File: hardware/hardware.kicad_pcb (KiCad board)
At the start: 2 copper layers, 85.5 x 50.5 mm, 22 parts, among them J1 Conn_01x05_Male, J2 DIN-5_180degree, SW1 SW_Push, SW2 SW_Push, U1 Teensy3.2, U2 TeensyAudioShield3.2, U3 6N138

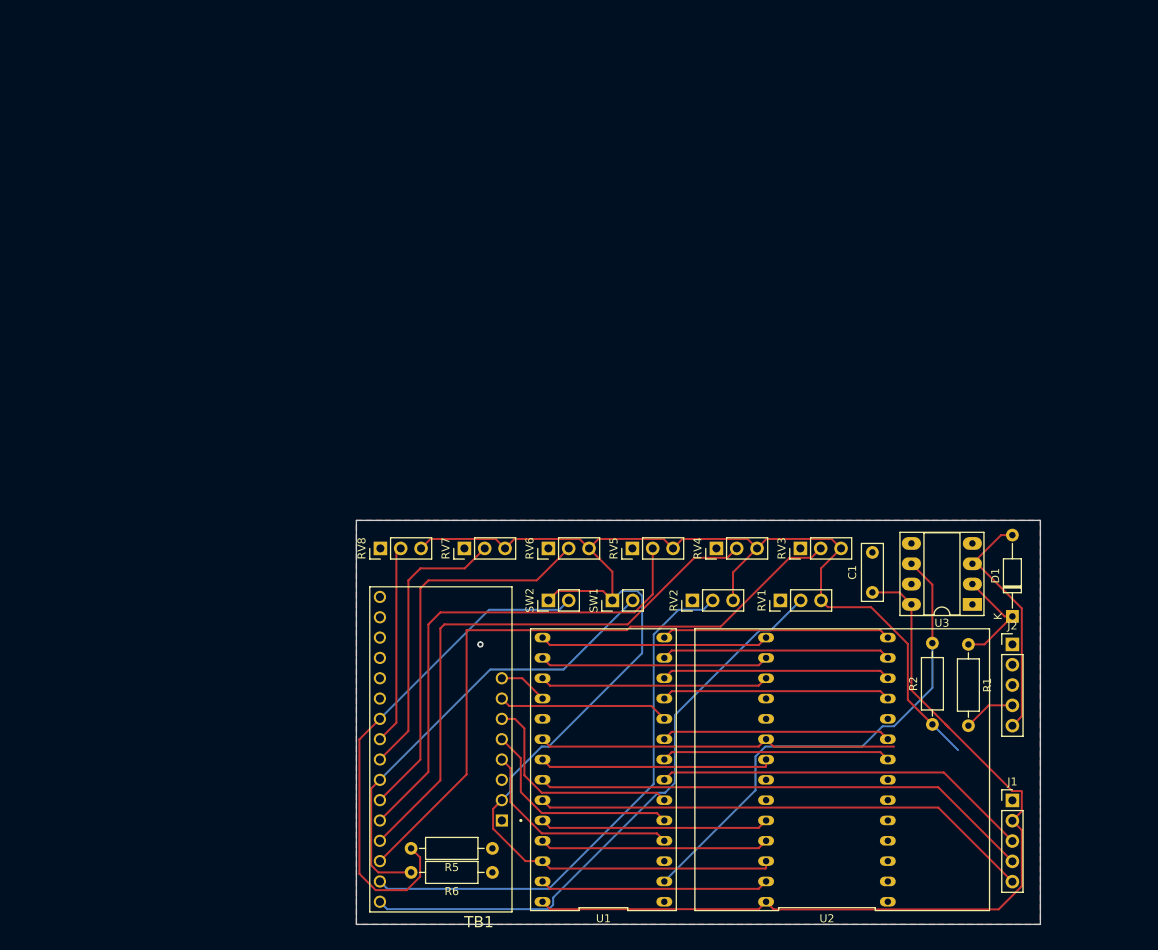
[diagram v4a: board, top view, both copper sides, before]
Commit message: V0.5 PCB for Hammond case with pcb mount pots
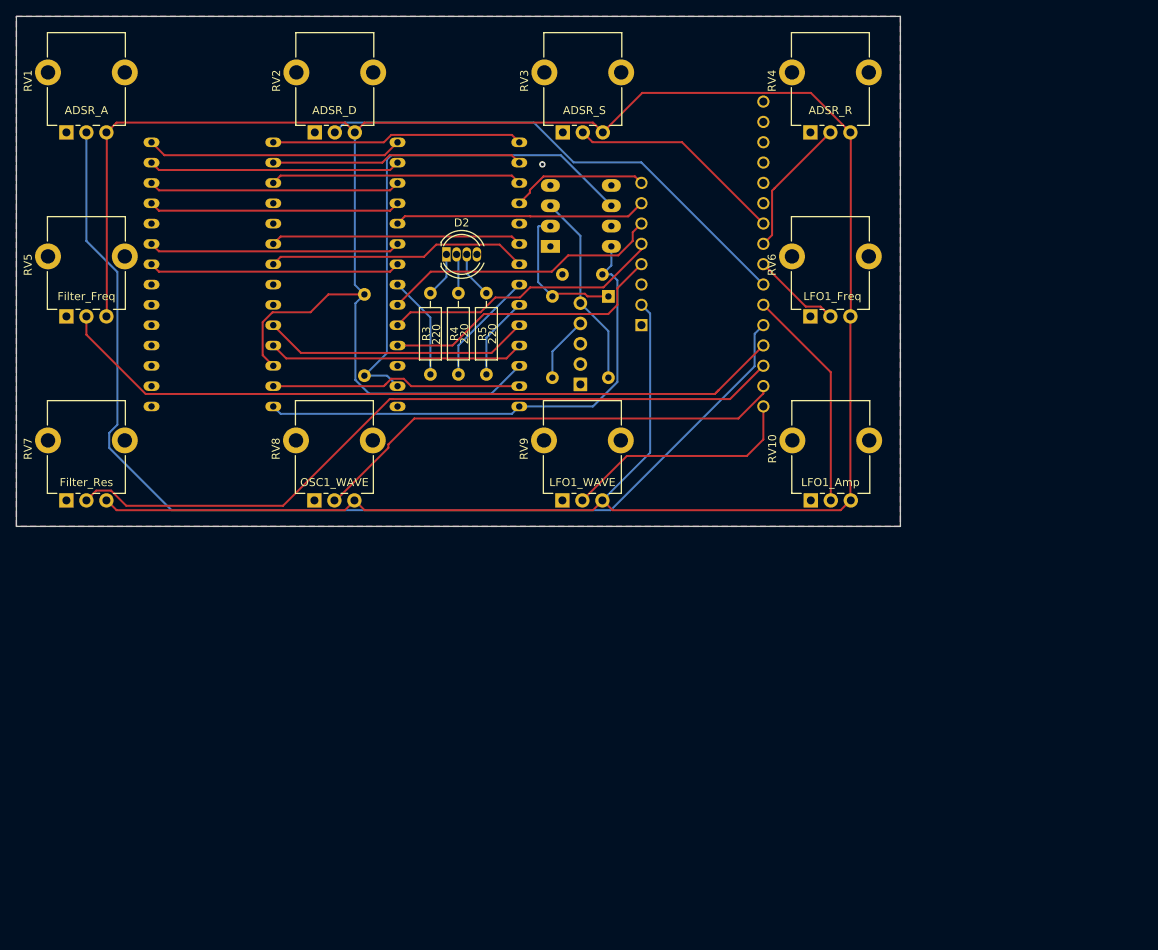
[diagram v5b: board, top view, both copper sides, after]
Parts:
- removed J2: DIN-5_180degree, Connector_PinHeader_2.54mm:PinHeader_1x05_P2.54mm_Vertical
- removed R6: 10k, Resistor_THT:R_Axial_DIN0207_L6.3mm_D2.5mm_P10.16mm_Horizontal
- removed SW1, SW2: SW_Push, Connector_PinHeader_2.54mm:PinHeader_1x02_P2.54mm_Vertical
- added D2: LED_RGBC, LED_THT:LED_D5.0mm-4_RGB, F.Cu at (99.8, 72.8)
- added R3: 220, Resistor_THT:R_Axial_DIN0207_L6.3mm_D2.5mm_P10.16mm_Horizontal, F.Cu at (97.8, 87.8)
- added R4: 220, Resistor_THT:R_Axial_DIN0207_L6.3mm_D2.5mm_P10.16mm_Horizontal, F.Cu at (101.2, 87.8)
- added RV10: R_POT, Potentiometer_THT:Potentiometer_Alpha_RD901F-40-00D_Single_Vertical_CircularHoles, F.Cu at (145.3, 103.5)
- added RV9: R_POT, Potentiometer_THT:Potentiometer_Alpha_RD901F-40-00D_Single_Vertical_CircularHoles, F.Cu at (114.2, 103.5)
- C1, D1, TB1, U1, U2, U3: moved to B.Cu
- J1: value Conn_01x05_Male -> DIN-5_180degree; moved to B.Cu
- R1: value 220 -> 470; moved to B.Cu
- R2: value 470 -> 220; moved to B.Cu
- R5: value 10k -> 220
- RV1, RV2, RV3, RV4, RV5, RV6, RV7, RV8: footprint Connector_PinHeader_2.54mm:PinHeader_1x03_P2.54mm_Vertical -> Potentiometer_THT:Potentiometer_Alpha_RD901F-40-00D_Single_Vertical_CircularHoles
- moved RV1 106.7 mm to (52.2, 57.5)
- moved U2 98.7 mm to (70.5, 75.2)
- moved R1 87.3 mm to (89.5, 77.8)
- moved RV5 76.5 mm to (52.2, 80.5)
- moved RV2 75.2 mm to (83.3, 57.5)
- moved J1 75.0 mm to (116.5, 89.0)
- moved R2 71.5 mm to (113.0, 78.0), turned to 270 degrees
- moved TB1 70.0 mm to (131.8, 72.7), turned to 0 degrees
- moved U3 69.2 mm to (112.8, 71.8), turned to 0 degrees
- moved U1 64.5 mm to (101.2, 75.2)
- moved D1 64.4 mm to (120.0, 78.0), turned to 270 degrees
- moved RV3 59.9 mm to (114.3, 57.5)
- moved R5 59.3 mm to (104.8, 87.8), turned to 90 degrees
- moved RV4 53.3 mm to (145.2, 57.5)
- moved C1 52.1 mm to (119.2, 75.2), turned to 180 degrees
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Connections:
- J1 pad 1: GND -> Net-(J1-Pad1)
- J1 pad 2: +5V -> Net-(J1-Pad2)
- J1 pad 3: /RGB_R -> Net-(J1-Pad3)
- J1 pad 4: /RGB_G -> Net-(J1-Pad4)
- J1 pad 5: /RGB_B -> Net-(D1-Pad2)
- R1 pad 1: Net-(D1-Pad1) -> +3V3
- R1 pad 2: Net-(J2-Pad4) -> /MIDI_IN
- R2 pad 1: +3V3 -> Net-(D1-Pad1)
- R2 pad 2: /MIDI_IN -> Net-(J1-Pad4)
- R5 pad 1: GND -> /RGB_B
- R5 pad 2: /LFO1_WAV -> Net-(D2-Pad3)
- RV1 pad 2: /Filter_Freq -> /m4
- RV2 pad 2: /Filter_Res -> /m6
- RV3 pad 2: /ADSR_Attack -> /m9
- RV4 pad 2: /ADSR_Decay -> /m8
- RV5 pad 2: /ADSR_Sustain -> /m3
- RV6 pad 2: /ADSR_Release -> /m7
- RV7 pad 2: /LFO1_Amp -> /m2
- RV8 pad 2: /LFO1_Freq -> /m1
- TB1 pad 10: /Filter_Res -> /m1
- TB1 pad 11: /ADSR_Attack -> /m2
- TB1 pad 12: /ADSR_Decay -> /m3
- TB1 pad 13: /ADSR_Sustain -> /m4
- TB1 pad 14: /ADSR_Release -> /m5
- TB1 pad 15: /OSC1_WAV -> /m6
- TB1 pad 16: /LFO1_Amp -> /m7
- TB1 pad 17: /LFO1_Freq -> /m8
- TB1 pad 18: /LFO1_WAV -> /m9
- TB1 pad 19: (no net) -> Net-(TB1-Pad19)
- TB1 pad 20: (no net) -> Net-(TB1-Pad20)
- TB1 pad 21: (no net) -> Net-(TB1-Pad21)
- TB1 pad 22: (no net) -> Net-(TB1-Pad22)
- TB1 pad 23: (no net) -> Net-(TB1-Pad23)
- TB1 pad 24: (no net) -> Net-(TB1-Pad24)
- TB1 pad 9: /Filter_Freq -> /m0
- U1 pad 19: (no net) -> Net-(U1-Pad19)
- U1 pad 3: (no net) -> Net-(U1-Pad3)
- U2 pad 10: (no net) -> Net-(U2-Pad10)
- U2 pad 18: (no net) -> Net-(U2-Pad18)
- U2 pad 19: (no net) -> Net-(U2-Pad19)
- U2 pad 2: (no net) -> Net-(U2-Pad2)
- U2 pad 22: (no net) -> Net-(U2-Pad22)
- U2 pad 23: (no net) -> Net-(U2-Pad23)
- U2 pad 3: (no net) -> Net-(U2-Pad3)
- U2 pad 4: (no net) -> Net-(U2-Pad4)
- U2 pad 5: (no net) -> Net-(U2-Pad5)
- U2 pad 6: (no net) -> Net-(U2-Pad6)
- U2 pad 7: (no net) -> Net-(U2-Pad7)
- U3 pad 1: (no net) -> Net-(U3-Pad1)
- U3 pad 4: (no net) -> Net-(U3-Pad4)
- U3 pad 7: (no net) -> Net-(U3-Pad7)
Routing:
- net +3V3: track 197.2 -> 366.2 mm
- net /m4: track 0.00 -> 138.4 mm
- net /m2: track 0.00 -> 93.4 mm
- net /m3: track 0.00 -> 92.8 mm
- net /ADSR_Attack: track 81.9 -> 0.00 mm
- net /Filter_Freq: track 74.5 -> 0.00 mm
- net /ADSR_Decay: track 70.9 -> 0.00 mm
- net /Filter_Res: track 67.9 -> 0.00 mm
- net /LFO1_WAV: track 63.3 -> 0.00 mm
- net /m6: track 0.00 -> 62.5 mm
- net /ADSR_Sustain: track 62.4 -> 0.00 mm
- net /m1: track 0.00 -> 60.3 mm
- net /OSC1_WAV: track 57.4 -> 0.00 mm
- net /RGB_B: track 63.0 -> 10.4 mm
- net /ADSR_Release: track 49.2 -> 0.00 mm
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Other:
- board size 85.5 x 50.5 mm -> 110.5 x 63.8 mm
- board text added: "ADSR_A"
- board text added: "ADSR_D"
- board text added: "ADSR_R"
- board text added: "ADSR_S"
- board text added: "Audio Adaptor"
- board text added: "CD74HC4067"
- board text added: "Filter_Freq"
- board text added: "Filter_Res"
- board text added: "LFO1_Amp"
- board text added: "LFO1_Freq"
- board text added: "LFO1_WAVE"
- board text added: "OSC1_WAVE"
- board text added: "Teensy 3.2"

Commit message: Redesign board to allow space for connectors
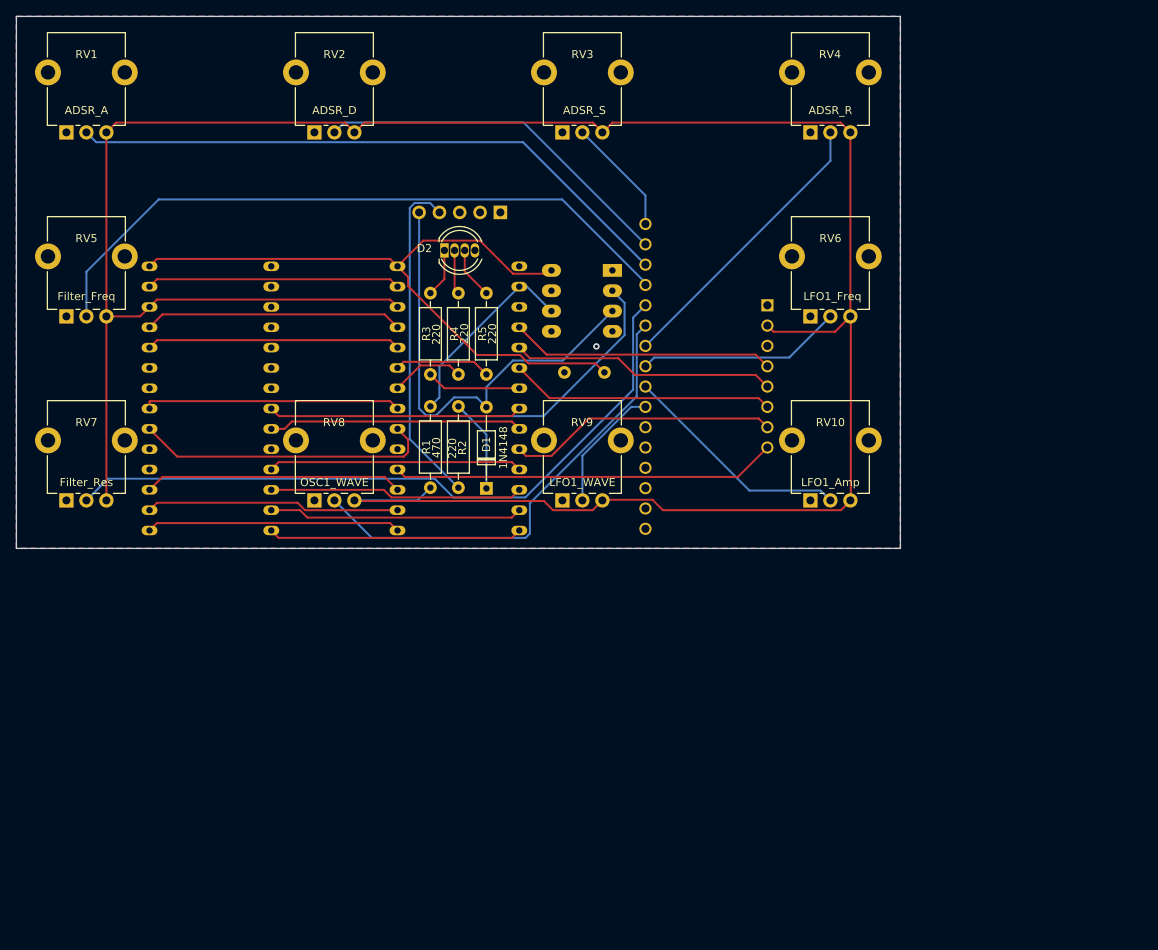
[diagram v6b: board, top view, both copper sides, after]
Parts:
- D1, R1, R2: moved to F.Cu
- moved RV8 62.1 mm to (83.2, 103.5)
- moved RV4 62.0 mm to (145.2, 57.5)
- moved RV9 46.0 mm to (114.2, 103.5)
- moved RV1 46.0 mm to (52.2, 57.5)
- moved RV10 46.0 mm to (145.2, 103.5)
- moved RV2 46.0 mm to (83.2, 57.5)
- moved RV3 46.0 mm to (114.2, 57.5)
- moved RV7 46.0 mm to (52.2, 103.5)
- moved D1 28.4 mm to (104.8, 102.0), turned to 90 degrees
- moved R1 25.5 mm to (97.8, 101.9), turned to 90 degrees
- moved J1 23.7 mm to (106.5, 67.5), turned to 90 degrees
- moved R2 18.1 mm to (101.2, 91.8)
- moved U2 15.5 mm to (70.2, 90.8), turned to 270 degrees
- moved U1 15.5 mm to (101.2, 90.8), turned to 270 degrees
- moved TB1 15.3 mm to (132.2, 88.0), turned to 180 degrees
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- renumbered RV7 to RV1, RV4 to RV10, RV8 to RV2, RV9 to RV3, RV2 to RV4, RV1 to RV7, RV10 to RV8, RV3 to RV9
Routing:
- net +3V3: track 366.2 -> 311.5 mm
- net /m4: track 138.4 -> 87.2 mm
- net /MIDI_IN: track 64.3 -> 24.9 mm
- net Net-(J1-Pad4): track 8.23 -> 41.9 mm
- net Net-(D1-Pad2): track 24.5 -> 56.9 mm
- net /MULT_SIG: track 17.2 -> 48.1 mm
- net /m5: track 27.9 -> 58.6 mm
- net /m6: track 62.5 -> 36.3 mm
- net Net-(D1-Pad1): track 18.3 -> 43.4 mm
- net +5V: track 63.9 -> 86.3 mm
- net /m2: track 93.4 -> 76.7 mm
- net /m0: track 29.9 -> 14.7 mm
- net /m1: track 60.3 -> 45.7 mm
- net /m7: track 11.1 -> 25.7 mm
- net /m8: track 17.4 -> 29.0 mm
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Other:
- board size 110.5 x 63.8 mm -> 110.5 x 66.5 mm
- board text added: "Robert Barnes"
- board text added: "Teensy Synth"
- board text added: "Version 0.5 2020-12-05"

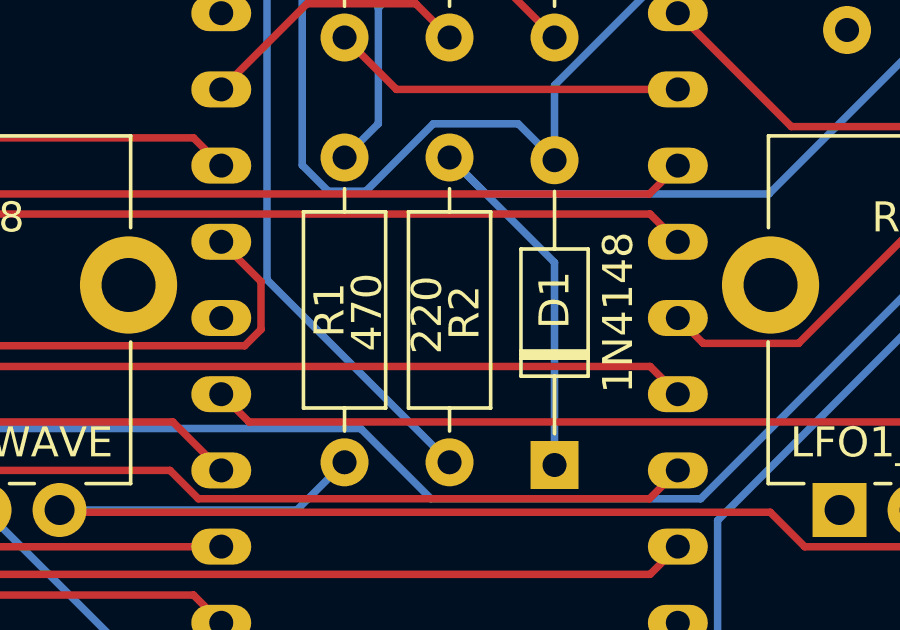
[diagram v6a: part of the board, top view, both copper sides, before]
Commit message: Add text to silks
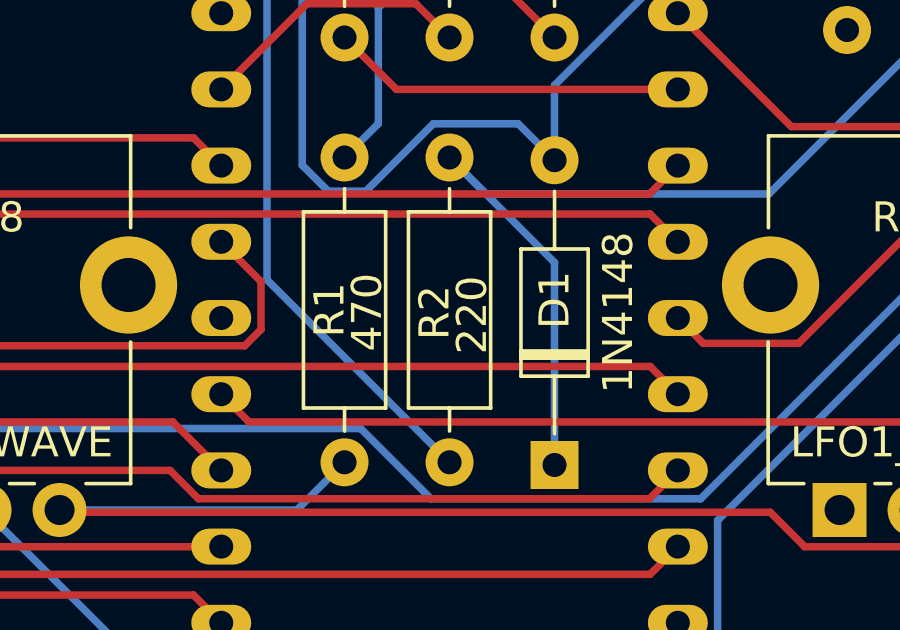
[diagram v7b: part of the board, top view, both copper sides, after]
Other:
- board text added: "MIDI Out"
